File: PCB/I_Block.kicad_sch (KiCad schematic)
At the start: 18 parts, among them IC32 TLV9351IDCKR, IC34 TLV9351IDCKR, IC36 TLV9351IDCKR, IC38 TLV9351IDCKR, IC42 TLV9351IDCKR, IC44 TLV9351IDCKR

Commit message: Revert "# Title: Summary, imperative, start upper case, don't end with a period"
This reverts commit 68e2e82ae65b044d3f55e91a7adcee939c25789e.
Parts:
- IC32, IC34, IC36, IC38, IC42, IC44: footprint TLV9351IDCKR:SOT65P210X110-5N -> SOT65P210X110-5N
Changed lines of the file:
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@@
       (effects (font (size 1.27 1.27)))
     )
-    (property "Footprint" "TLV9351IDCKR:SOT65P210X110-5N" (at 126.365 -23.8 0)
+    (property "Footprint" "SOT65P210X110-5N" (at 126.365 -23.8 0)
       (effects (font (size 1.27 1.27)) (justify left top) hide)
     )
@@
       (effects (font (size 1.27 1.27)))
     )
-    (property "Footprint" "TLV9351IDCKR:SOT65P210X110-5N" (at 126.365 40.335 0)
+    (property "Footprint" "SOT65P210X110-5N" (at 126.365 40.335 0)
       (effects (font (size 1.27 1.27)) (justify left top) hide)
     )
@@
       (effects (font (size 1.27 1.27)))
     )
-    (property "Footprint" "TLV9351IDCKR:SOT65P210X110-5N" (at 126.365 -2.845 0)
+    (property "Footprint" "SOT65P210X110-5N" (at 126.365 -2.845 0)
       (effects (font (size 1.27 1.27)) (justify left top) hide)
     )
@@
       (effects (font (size 1.27 1.27)))
     )
-    (property "Footprint" "TLV9351IDCKR:SOT65P210X110-5N" (at 125.73 60.655 0)
+    (property "Footprint" "SOT65P210X110-5N" (at 125.73 60.655 0)
       (effects (font (size 1.27 1.27)) (justify left top) hide)
     )
@@
       (effects (font (size 1.27 1.27)))
     )
-    (property "Footprint" "TLV9351IDCKR:SOT65P210X110-5N" (at 125.73 80.34 0)
+    (property "Footprint" "SOT65P210X110-5N" (at 125.73 80.34 0)
       (effects (font (size 1.27 1.27)) (justify left top) hide)
     )
@@
       (effects (font (size 1.27 1.27)))
     )
-    (property "Footprint" "TLV9351IDCKR:SOT65P210X110-5N" (at 126.365 18.11 0)
-      (effects (font (size 1.27 1.27)) (justify left top) hide)
-    )
+    (property "Footprint" "SOT65P210X110-5N" (at 126.365 18.11 0)
+      (effects (font (size 1.27 1.27)) (justify left top) hide)
+    )

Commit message: Revert "Revert "# Title: Summary, imperative, start upper case, don't end with a period""
This reverts commit 3a20dd9da141c7cb1bae8077342d3450242b15f5.
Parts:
- IC32, IC34, IC36, IC38, IC42, IC44: footprint SOT65P210X110-5N -> TLV9351IDCKR:SOT65P210X110-5N
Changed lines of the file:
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@@
       (effects (font (size 1.27 1.27)))
     )
-    (property "Footprint" "SOT65P210X110-5N" (at 126.365 -23.8 0)
+    (property "Footprint" "TLV9351IDCKR:SOT65P210X110-5N" (at 126.365 -23.8 0)
       (effects (font (size 1.27 1.27)) (justify left top) hide)
     )
@@
       (effects (font (size 1.27 1.27)))
     )
-    (property "Footprint" "SOT65P210X110-5N" (at 126.365 40.335 0)
+    (property "Footprint" "TLV9351IDCKR:SOT65P210X110-5N" (at 126.365 40.335 0)
       (effects (font (size 1.27 1.27)) (justify left top) hide)
     )
@@
       (effects (font (size 1.27 1.27)))
     )
-    (property "Footprint" "SOT65P210X110-5N" (at 126.365 -2.845 0)
+    (property "Footprint" "TLV9351IDCKR:SOT65P210X110-5N" (at 126.365 -2.845 0)
       (effects (font (size 1.27 1.27)) (justify left top) hide)
     )
@@
       (effects (font (size 1.27 1.27)))
     )
-    (property "Footprint" "SOT65P210X110-5N" (at 125.73 60.655 0)
+    (property "Footprint" "TLV9351IDCKR:SOT65P210X110-5N" (at 125.73 60.655 0)
       (effects (font (size 1.27 1.27)) (justify left top) hide)
     )
@@
       (effects (font (size 1.27 1.27)))
     )
-    (property "Footprint" "SOT65P210X110-5N" (at 125.73 80.34 0)
+    (property "Footprint" "TLV9351IDCKR:SOT65P210X110-5N" (at 125.73 80.34 0)
       (effects (font (size 1.27 1.27)) (justify left top) hide)
     )
@@
       (effects (font (size 1.27 1.27)))
     )
-    (property "Footprint" "SOT65P210X110-5N" (at 126.365 18.11 0)
-      (effects (font (size 1.27 1.27)) (justify left top) hide)
-    )
+    (property "Footprint" "TLV9351IDCKR:SOT65P210X110-5N" (at 126.365 18.11 0)
+      (effects (font (size 1.27 1.27)) (justify left top) hide)
+    )

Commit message: Finalized generalized design
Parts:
- removed R31, R35, R39, R41, R50: 2.5k, symbol Device:R
- removed R32, R36, R40, R42, R51: 10k, symbol Device:R
- added R25, R27, R28, R29, R30: CRCW12102K49FKEA, RESC3225X60N, symbol CRCW12102K49FKEA:CRCW12102K49FKEA
- added R31, R33, R34, R35, R36: RMCF1210FT10K0, RESC3225X70N, symbol RMCF1210FT10K0:RMCF1210FT10K0
- R26: renamed from R55; value 2.5k -> CRCW12102K49FKEA; footprint (none) -> RESC3225X60N; symbol Device:R -> CRCW12102K49FKEA:CRCW12102K49FKEA; Height (none) -> 0.6; Manufacturer_Name (none) -> Vishay; Manufacturer_Part_Number (none) -> CRCW12102K49FKEA; Mouser Part Number (none) -> 71-CRCW1210-2.49K-E3; Mouser Price/Stock (none) -> http://www.mouser.com/Search/ProductDetail.aspx?qs=u0pLYIWD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
- R32: renamed from R56; value 10k -> RMCF1210FT10K0; footprint (none) -> RESC3225X70N; symbol Device:R -> RMCF1210FT10K0:RMCF1210FT10K0; Height (none) -> 0.7; Manufacturer_Name (none) -> Stackpole Electronics, Inc.; Manufacturer_Part_Number (none) -> RMCF1210FT10K0; Mouser Part Number (none) -> 708-RMCF1210FT10K0; Mouser Price/Stock (none) -> https://www.mouser.com/ProductDetail/SEI-Stackpole/RMCF1210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
- renumbered IC42 to IC19, IC44 to IC20, IC38 to IC21, IC36 to IC22, IC34 to IC23, IC32 to IC24
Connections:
- net GND: now also R26.2, R25.2, R27.2, R28.2, R29.2, R30.2; no longer R26.1
- net I_ACT_1: now also R26.1, R32.2; no longer R26.2, R32.1
- net I_ACT_2: now also R25.1, R31.2
- net I_ACT_3: now also R30.1, R36.2
- net I_ACT_4: now also R29.1, R35.2
- net I_ACT_5: now also R28.1, R34.2
- net I_ACT_6: now also R27.1, R33.2
- net at IC22.3 (IN-), IC22.4 (OUT): now also R34.1
- net at IC21.3 (IN-), IC21.4 (OUT): now also R33.1
- net at IC24.3 (IN-), IC24.4 (OUT): now also R36.1
- net at IC23.3 (IN-), IC23.4 (OUT): now also R35.1
- net at IC20.3 (IN-), IC20.4 (OUT): now also R32.1; no longer R32.2
- net at IC19.3 (IN-), IC19.4 (OUT): now also R31.1
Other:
- moved on the sheet: IC19, IC20, IC21, IC22, IC23, IC24

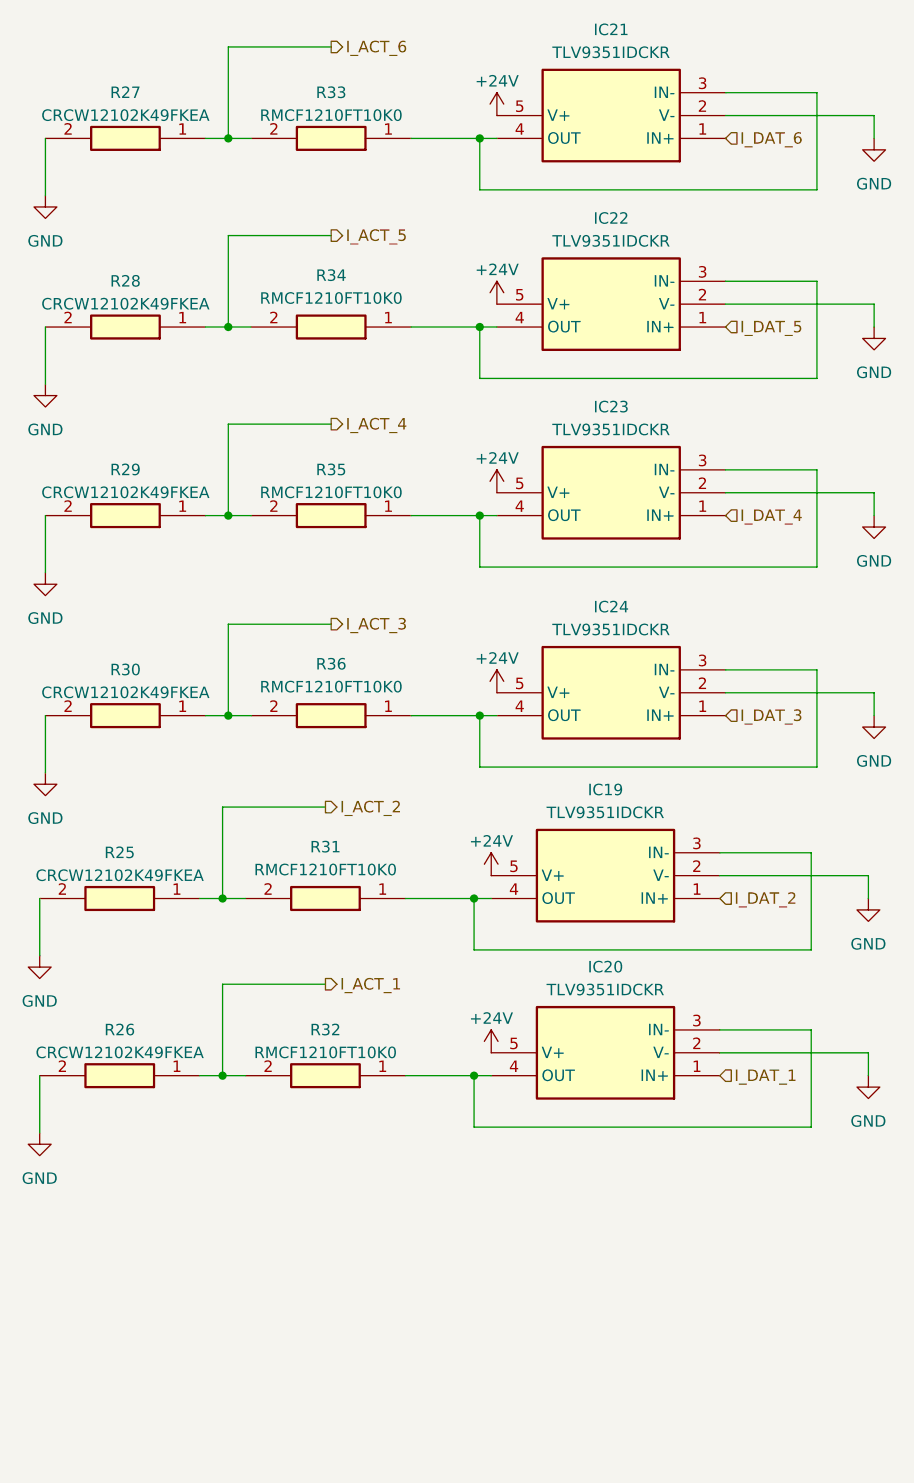
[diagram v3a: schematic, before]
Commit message: Redesigned, to utilize the ESP32 as the basis
* Implemented EEPROM
* Implemented RTC
* Implemented RS232 and 485
* Implemented CANBus
* Implemented everything
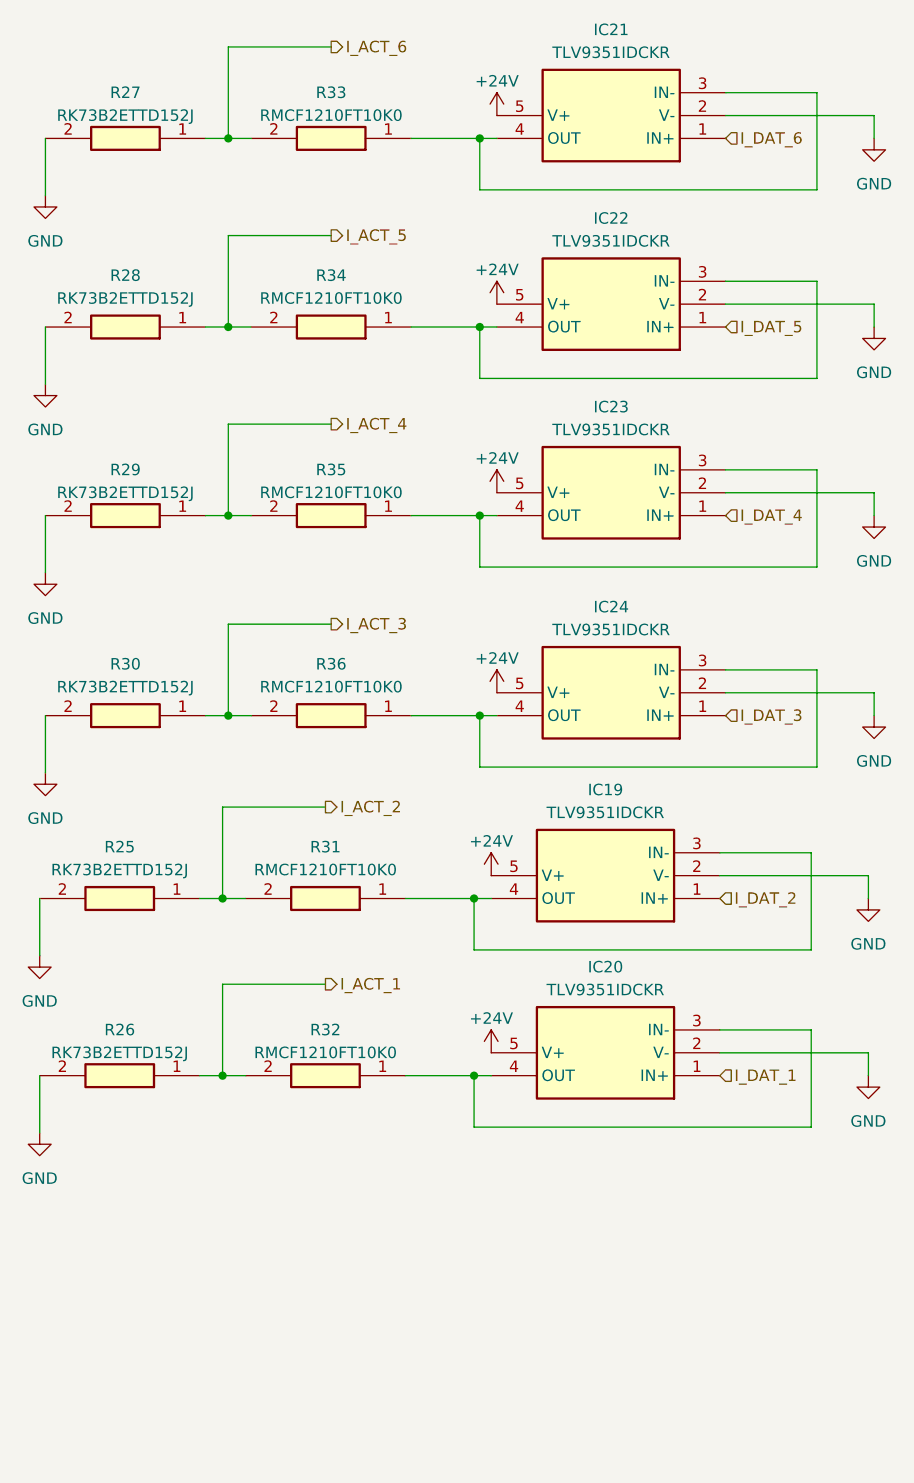
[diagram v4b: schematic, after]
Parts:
- R25, R26, R27, R28, R29, R30: value CRCW12102K49FKEA -> RK73B2ETTD152J; footprint RESC3225X60N -> RESC3226X70N; symbol CRCW12102K49FKEA:CRCW12102K49FKEA -> RK73B2ETTD152J:RK73B2ETTD152J; Height 0.6 -> 0.7; Manufacturer_Name Vishay -> KOA Speer; Manufacturer_Part_Number CRCW12102K49FKEA -> RK73B2ETTD152J; Mouser Part Number 71-CRCW1210-2.49K-E3 -> 660-RK73B2ETTD152J; Mouser Price/Stock http://www.mouser.com/Search/ProductDetail.aspx?qs=u0pLYIWD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 -> https://www.mouser.co.uk/ProductDetail/KOA-Speer/RK73B2ETTD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
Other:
- company: (none) -> UPB - FIIR - Roboți și sisteme de producție

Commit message: Implemented Output block in PCB Started implementation of Input block in PCB
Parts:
- R25, R26, R27, R28, R29, R30: footprint RESC3226X70N -> RK73B2ETTD152J:RESC3226X70N
- R31, R32, R33, R34, R35, R36: footprint RESC3225X70N -> RMCF1210FT10K0:RESC3225X70N
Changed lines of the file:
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@@
       (effects (font (size 1.27 1.27)))
     )
-    (property "Footprint" "RESC3226X70N" (at 77.47 28.905 0)
+    (property "Footprint" "RK73B2ETTD152J:RESC3226X70N" (at 77.47 28.905 0)
       (effects (font (size 1.27 1.27)) (justify left top) hide)
     )
@@
       (effects (font (size 1.27 1.27)))
     )
-    (property "Footprint" "RESC3225X70N" (at 100.965 -55.55 0)
+    (property "Footprint" "RMCF1210FT10K0:RESC3225X70N" (at 100.965 -55.55 0)
       (effects (font (size 1.27 1.27)) (justify left top) hide)
     )
@@
       (effects (font (size 1.27 1.27)))
     )
-    (property "Footprint" "RESC3225X70N" (at 100.965 -34.595 0)
+    (property "Footprint" "RMCF1210FT10K0:RESC3225X70N" (at 100.965 -34.595 0)
       (effects (font (size 1.27 1.27)) (justify left top) hide)
     )
@@
       (effects (font (size 1.27 1.27)))
     )
-    (property "Footprint" "RESC3225X70N" (at 100.33 28.905 0)
+    (property "Footprint" "RMCF1210FT10K0:RESC3225X70N" (at 100.33 28.905 0)
       (effects (font (size 1.27 1.27)) (justify left top) hide)
     )
@@
       (effects (font (size 1.27 1.27)))
     )
-    (property "Footprint" "RESC3225X70N" (at 100.33 48.59 0)
+    (property "Footprint" "RMCF1210FT10K0:RESC3225X70N" (at 100.33 48.59 0)
       (effects (font (size 1.27 1.27)) (justify left top) hide)
     )
@@
       (effects (font (size 1.27 1.27)))
     )
-    (property "Footprint" "RESC3225X70N" (at 100.965 -13.64 0)
+    (property "Footprint" "RMCF1210FT10K0:RESC3225X70N" (at 100.965 -13.64 0)
       (effects (font (size 1.27 1.27)) (justify left top) hide)
     )
@@
       (effects (font (size 1.27 1.27)))
     )
-    (property "Footprint" "RESC3225X70N" (at 100.965 8.585 0)
+    (property "Footprint" "RMCF1210FT10K0:RESC3225X70N" (at 100.965 8.585 0)
       (effects (font (size 1.27 1.27)) (justify left top) hide)
     )
@@
       (effects (font (size 1.27 1.27)))
     )
-    (property "Footprint" "RESC3226X70N" (at 78.105 -13.64 0)
+    (property "Footprint" "RK73B2ETTD152J:RESC3226X70N" (at 78.105 -13.64 0)
       (effects (font (size 1.27 1.27)) (justify left top) hide)
     )
@@
       (effects (font (size 1.27 1.27)))
     )
-    (property "Footprint" "RESC3226X70N" (at 78.105 -55.55 0)
+    (property "Footprint" "RK73B2ETTD152J:RESC3226X70N" (at 78.105 -55.55 0)
       (effects (font (size 1.27 1.27)) (justify left top) hide)
     )
@@
       (effects (font (size 1.27 1.27)))
     )
-    (property "Footprint" "RESC3226X70N" (at 77.47 48.59 0)
+    (property "Footprint" "RK73B2ETTD152J:RESC3226X70N" (at 77.47 48.59 0)
       (effects (font (size 1.27 1.27)) (justify left top) hide)
     )
@@
       (effects (font (size 1.27 1.27)))
     )
-    (property "Footprint" "RESC3226X70N" (at 78.105 -34.595 0)
+    (property "Footprint" "RK73B2ETTD152J:RESC3226X70N" (at 78.105 -34.595 0)
       (effects (font (size 1.27 1.27)) (justify left top) hide)
     )
@@
       (effects (font (size 1.27 1.27)))
     )
-    (property "Footprint" "RESC3226X70N" (at 78.105 8.585 0)
-      (effects (font (size 1.27 1.27)) (justify left top) hide)
-    )
+    (property "Footprint" "RK73B2ETTD152J:RESC3226X70N" (at 78.105 8.585 0)
+      (effects (font (size 1.27 1.27)) (justify left top) hide)
+    )
